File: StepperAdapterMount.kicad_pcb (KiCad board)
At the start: 2 copper layers, 14.5 x 14 mm, 1 part, among them M1 StepperMotor_4.7mm_Sanyo_ultr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

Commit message: Update 3d models in library
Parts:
- added H1: M2 MountingHole, MountingHole:MountingHole_2.2mm_M2_ISO7380_Pad, F.Cu at (94.8, 179.5)
- added H2: M2 MountingHole, MountingHole:MountingHole_2.2mm_M2_ISO7380_Pad, F.Cu at (94.8, 189.5)
- added REF**: Jushuo_AFC07-S06FCA-00_1x6-1MP_P0.50_Horizontal, Connector_FFC-FPC:Jushuo_AFC07-S06FCA-00_1x6-1MP_P0.50_Horizontal, F.Cu at (75.3, 184.5)
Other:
- board size 14.5 x 14 mm -> 14.5 x 15 mm
- board text removed: "anyo Ultra-mini 4.7mm Stepper"

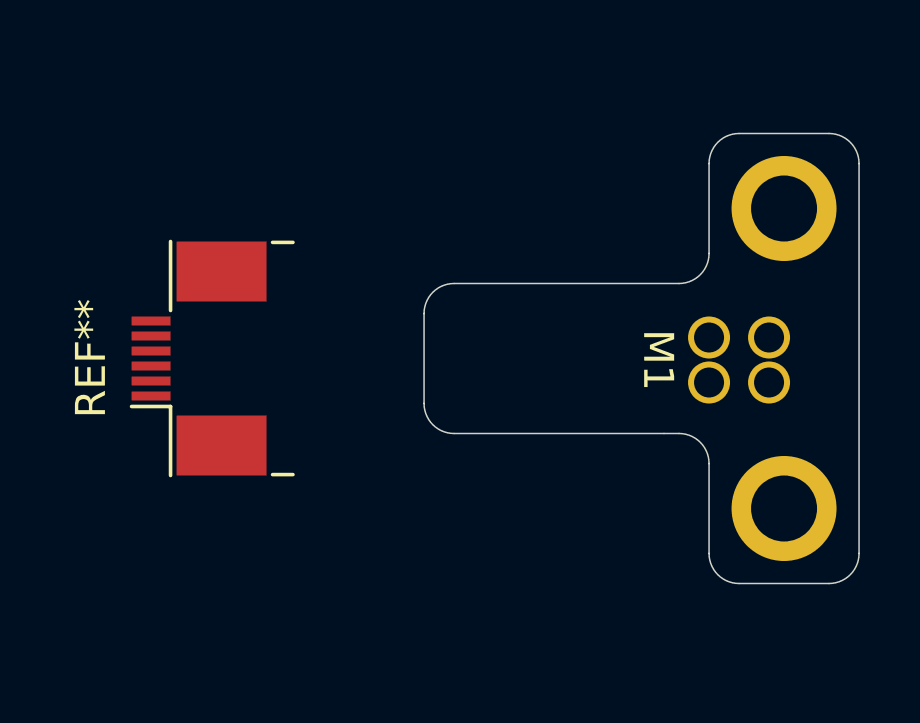
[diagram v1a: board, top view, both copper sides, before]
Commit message: Updated board shape
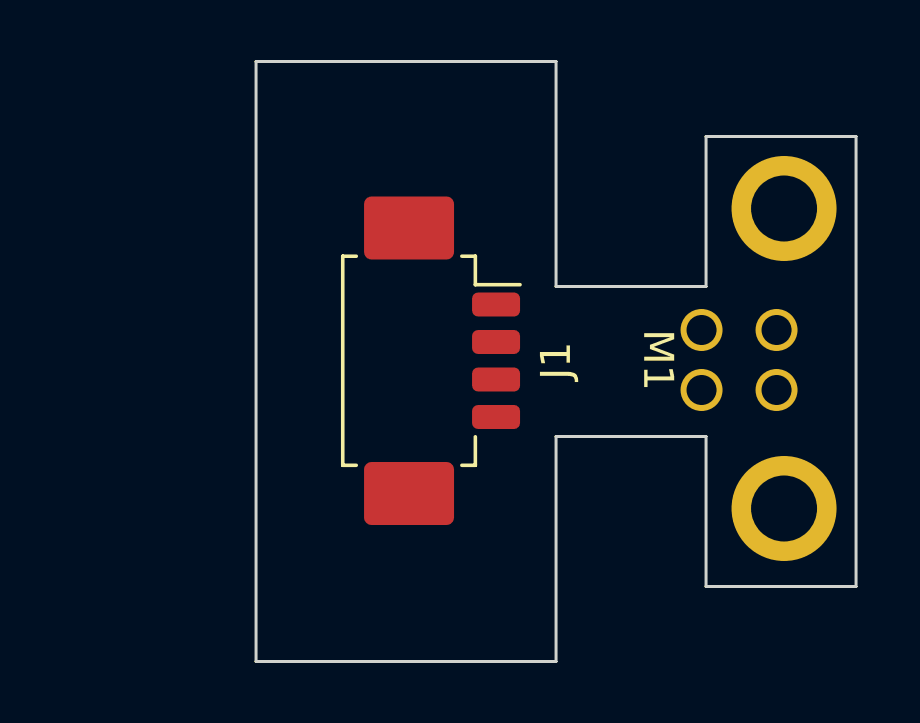
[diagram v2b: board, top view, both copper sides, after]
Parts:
- removed REF**: Jushuo_AFC07-S06FCA-00_1x6-1MP_P0.50_Horizontal, Connector_FFC-FPC:Jushuo_AFC07-S06FCA-00_1x6-1MP_P0.50_Horizontal
- added J1: Conn_01x04, Connector_Molex:Molex_PicoBlade_53261-0471_1x04-1MP_P1.25mm_Horizontal, F.Cu at (82.8, 184.6)
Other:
- board size 14.5 x 15 mm -> 20 x 20 mm

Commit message: v1.0
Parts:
- removed H1, H2: M2 MountingHole, MountingHole:MountingHole_2.2mm_M2_ISO7380_Pad
- added J2: Conn_01x04, Connector_PinHeader_2.54mm:PinHeader_1x04_P2.54mm_Vertical, B.Cu at (61.8, 215.0)
- added J3: Conn_01x04, Connector_PinHeader_2.54mm:PinHeader_1x04_P2.54mm_Vertical, B.Cu at (49.1, 199.7)
- added J4: Conn_01x04, Connector_PinHeader_2.54mm:PinHeader_1x04_P2.54mm_Vertical, B.Cu at (49.1, 215.0)
- added M2: StepperMotor_8mm_i500212644, AC-kicad-library:StepperMotor_8mm_i500212644, F.Cu at (43.4, 207.4)
- J1: footprint Connector_Molex:Molex_PicoBlade_53261-0471_1x04-1MP_P1.25mm_Horizontal -> Connector_PinHeader_2.54mm:PinHeader_1x04_P2.54mm_Vertical; moved to B.Cu
- moved M1 40.0 mm to (60.5, 207.4)
- moved J1 25.9 mm to (61.8, 199.7), turned to 90 degrees
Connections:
- J1 pad 1: unconnected-(J1-Pin_1-Pad1) -> /A1+
- J1 pad 4: unconnected-(J1-Pin_4-Pad4) -> /B1+
- M1 pad 1: unconnected-(M1-A+-Pad1) -> /A1+
- M1 pad 2: unconnected-(M1-A--Pad2) -> /A1-
- M1 pad 3: unconnected-(M1-B+-Pad3) -> /B1+
- M1 pad 4: unconnected-(M1-B--Pad4) -> /B1-
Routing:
- net /A2-: track 0.00 -> 11.1 mm
- net /B1+: track 0.00 -> 10.4 mm
- net /B1-: track 0.00 -> 10.4 mm
- net /A2+: track 0.00 -> 9.76 mm
- net /B2+: track 0.00 -> 7.67 mm
- net /A1+: track 0.00 -> 6.69 mm
- net /A1-: track 0.00 -> 6.59 mm
- net /B2-: track 0.00 -> 6.32 mm
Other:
- board size 20 x 20 mm -> 25.4 x 20.3 mm
- board text added: "A+"
- board text added: "A-"
- board text added: "B+"
- board text added: "B-"
- board text added: "V-Score"

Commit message: changed library for smaller hole size
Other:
- board text added: "V1.1"
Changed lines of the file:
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@@
 		(grid_origin 94.85 184.5)
 		(pcbplotparams
-			(layerselection 0x00812fc_ffffffff)
+			(layerselection 0x00012fc_ffffffff)
 			(plot_on_all_layers_selection 0x0000000_00000000)
 			(disableapertmacros no)
@@
 			)
 		)
+		(fp_text user "B-"
+			(at 1.85 -2.45 90)
+			(unlocked yes)
+			(layer "F.SilkS")
+			(effects
+				(font
+					(size 1 1)
+					(thickness 0.1)
+				)
+				(justify left bottom)
+			)
+		)
+		(fp_text user "A+"
+			(at 0.95 2 90)
+			(unlocked yes)
+			(layer "F.SilkS")
+			(effects
+				(font
+					(size 1 1)
+					(thickness 0.1)
+				)
+				(justify left bottom)
+			)
+		)
 		(fp_text user "A-"
 			(at 0.95 -1.15 90)
-			(unlocked yes)
-			(layer "F.SilkS")
-			(effects
-				(font
-					(size 1 1)
-					(thickness 0.1)
-				)
-				(justify left bottom)
-			)
-		)
-		(fp_text user "B-"
-			(at 1.85 -2.45 90)
-			(unlocked yes)
-			(layer "F.SilkS")
-			(effects
-				(font
-					(size 1 1)
-					(thickness 0.1)
-				)
-				(justify left bottom)
-			)
-		)
-		(fp_text user "A+"
-			(at 0.95 2 90)
 			(unlocked yes)
 			(layer "F.SilkS")
@@
 				(extension_offset 0.5)
 			)
+		)
+		(dimension
+			(type orthogonal)
+			(layer "Dwgs.User")
+			(pts
+				(xy 43.315 209.46) (xy 43.515 208.06)
+			)
+			(height 6.2)
+			(orientation 1)
+			(gr_text "1.4000 mm"
+				(at 48.365 208.76 90)
+				(layer "Dwgs.User")
+				(effects
+					(font
+						(size 1 1)
+						(thickness 0.15)
+					)
+				)
+			)
+			(format
+				(prefix "")
+				(suffix "")
+				(units 3)
+				(units_format 1)
+				(precision 4)
+			)
+			(style
+				(thickness 0.1)
+				(arrow_length 0.5)
+				(text_position_mode 0)
+				(extension_height 0.58642)
+				(extension_offset 0.5) keep_text_aligned)
 		)
 		(dimension
@@
 				(extension_offset 0.5) keep_text_aligned)
 		)
-		(dimension
-			(type orthogonal)
-			(layer "Dwgs.User")
-			(pts
-				(xy 43.315 209.46) (xy 43.515 208.06)
-			)
-			(height 6.2)
-			(orientation 1)
-			(gr_text "1.4000 mm"
-				(at 48.365 208.76 90)
-				(layer "Dwgs.User")
-				(effects
-					(font
-						(size 1 1)
-						(thickness 0.15)
-					)
-				)
-			)
-			(format
-				(prefix "")
-				(suffix "")
-				(units 3)
-				(units_format 1)
-				(precision 4)
-			)
-			(style
-				(thickness 0.1)
-				(arrow_length 0.5)
-				(text_position_mode 0)
-				(extension_height 0.58642)
-				(extension_offset 0.5) keep_text_aligned)
-		)
 		(pad "1" thru_hole circle
 			(at -0.1 2.1 180)
-			(size 1.3 1.3)
-			(drill 0.9)
+			(size 1.25 1.25)
+			(drill 0.8)
 			(layers "*.Cu" "*.Mask")
 			(remove_unused_layers no)
@@
 		(pad "2" thru_hole circle
 			(at -0.1 -0.7 180)
-			(size 1.3 1.3)
-			(drill 0.9)
+			(size 1.25 1.25)
+			(drill 0.8)
 			(layers "*.Cu" "*.Mask")
 			(remove_unused_layers no)
@@
 		(pad "3" thru_hole circle
 			(at 0.1 0.7 180)
-			(size 1.3 1.3)
-			(drill 0.9)
+			(size 1.25 1.25)
+			(drill 0.8)
 			(layers "*.Cu" "*.Mask")
 			(remove_unused_layers no)
@@
 		(pad "4" thru_hole circle
 			(at 0.1 -2.1 180)
-			(size 1.3 1.3)
-			(drill 0.9)
+			(size 1.25 1.25)
+			(drill 0.8)
 			(layers "*.Cu" "*.Mask")
 			(remove_unused_layers no)
@@
 			(layer "Dwgs.User")
 		)
+		(fp_text user "A+"
+			(at 1.05 -3.9 -90)
+			(unlocked yes)
+			(layer "F.SilkS")
+			(effects
+				(font
+					(size 1 1)
+					(thickness 0.1)
+				)
+				(justify left bottom)
+			)
+		)
+		(fp_text user "B+"
+			(at -2.1 -3.9 -90)
+			(unlocked yes)
+			(layer "F.SilkS")
+			(effects
+				(font
+					(size 1 1)
+					(thickness 0.1)
+				)
+				(justify left bottom)
+			)
+		)
 		(fp_text user "B-"
 			(at -2.1 2 -90)
@@
 		(fp_text user "A-"
 			(at 1.05 2 -90)
-			(unlocked yes)
-			(layer "F.SilkS")
-			(effects
-				(font
-					(size 1 1)
-					(thickness 0.1)
-				)
-				(justify left bottom)
-			)
-		)
-		(fp_text user "B+"
-			(at -2.1 -3.9 -90)
-			(unlocked yes)
-			(layer "F.SilkS")
-			(effects
-				(font
-					(size 1 1)
-					(thickness 0.1)
-				)
-				(justify left bottom)
-			)
-		)
-		(fp_text user "A+"
-			(at 1.05 -3.9 -90)
 			(unlocked yes)
 			(layer "F.SilkS")
@@
 		)
 		(fp_text user "${REFERENCE}"
-			(at 0 -3.81 360)
+			(at 0 -3.81 0)
 			(layer "B.Fab")
 			(effects
@@
 		)
 		(fp_text user "${REFERENCE}"
-			(at 0 -3.81 360)
+			(at 0 -3.81 0)
 			(layer "B.Fab")
 			(effects
@@
 		)
 		(fp_text user "${REFERENCE}"
-			(at 0 -3.81 360)
+			(at 0 -3.81 0)
 			(layer "B.Fab")
 			(effects
@@
 		)
 		(fp_text user "${REFERENCE}"
-			(at 0 -3.81 360)
+			(at 0 -3.81 0)
 			(layer "B.Fab")
 			(effects
@@
 			)
 			(justify left bottom)
+		)
+	)
+	(gr_text "V1.1"
+		(at 52.94 205.836 -90)
+		(layer "F.SilkS")
+		(effects
+			(font
+				(size 1 1)
+				(thickness 0.15)
+			)
+			(justify left bottom)

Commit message: updated hole spacing for v1.2
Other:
- board text added: "V1.2"
- board text removed: "V1.1"
